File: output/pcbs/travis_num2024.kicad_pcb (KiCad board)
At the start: 2 copper layers, 85.2 x 132.8 mm, 91 parts

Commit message: numpad cap and firmware
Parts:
- C1: value 470uF 10V -> 6.3V 1000uF; footprint CP_Elec_6.3x7.7 -> Capacitor_THT:C_Radial_D6.3mm_H11.0mm_P2.50mm
- moved C1 1.25 mm to (37.0, 93.6), turned to 270 degrees
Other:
- board text added: "2024.06.20"
- board text removed: "2024.05.15"

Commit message: rotated
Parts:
- moved D15 20.8 mm to (106.3, 198.4), turned to 180 degrees
- moved D16 20.8 mm to (106.3, 158.3), turned to 180 degrees
- moved D1 20.8 mm to (41.6, 206.1), turned to 90 degrees
- moved D2 20.8 mm to (31.6, 186.1), turned to 90 degrees
- moved D3 20.8 mm to (31.6, 166.0), turned to 90 degrees
- moved D4 20.8 mm to (31.6, 146.0), turned to 90 degrees
- moved D5 20.8 mm to (31.6, 125.9), turned to 90 degrees
- moved D10 20.8 mm to (71.7, 206.1), turned to 90 degrees
- moved D11 20.8 mm to (71.7, 186.1), turned to 90 degrees
- moved D12 20.8 mm to (71.7, 166.0), turned to 90 degrees
- moved D13 20.8 mm to (71.7, 146.0), turned to 90 degrees
- moved D14 20.8 mm to (71.7, 125.9), turned to 90 degrees
- moved D17 20.8 mm to (91.7, 125.9), turned to 90 degrees
- moved D6 20.8 mm to (51.6, 186.1), turned to 90 degrees
- moved D7 20.8 mm to (51.6, 166.0), turned to 90 degrees
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
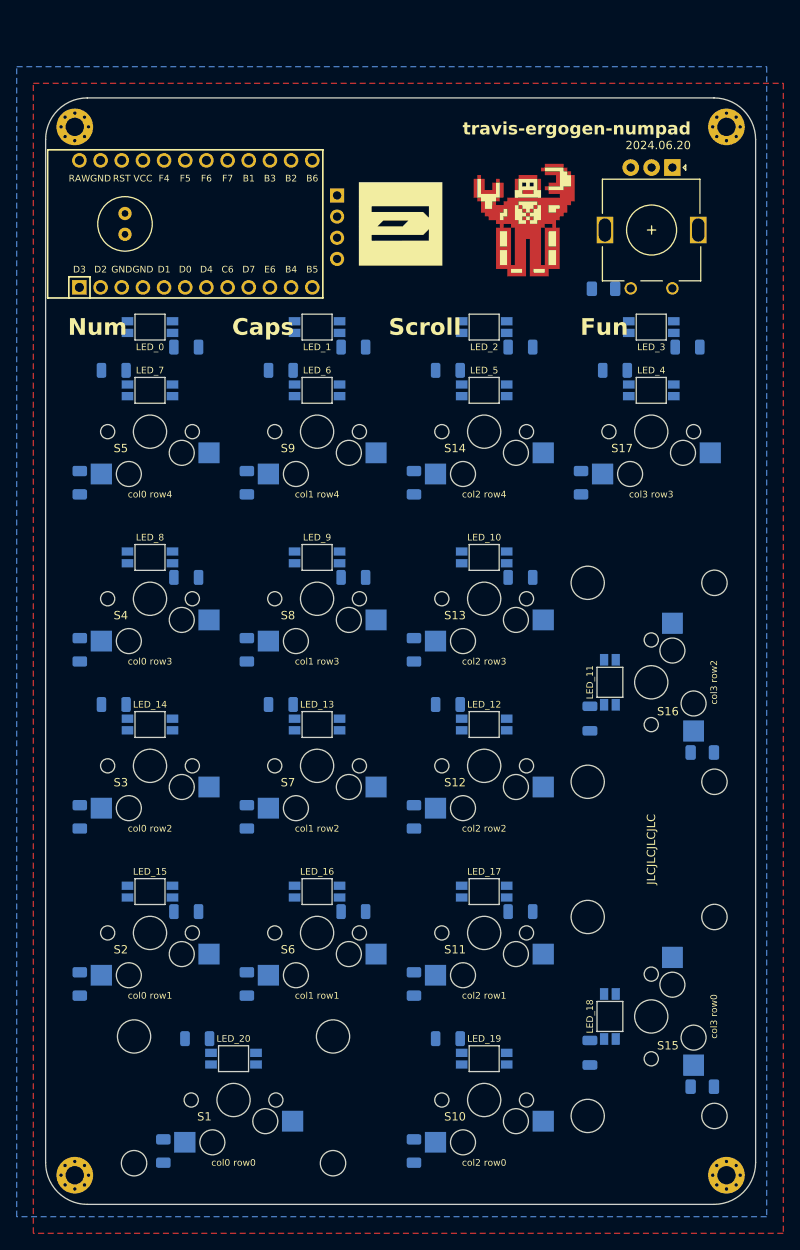
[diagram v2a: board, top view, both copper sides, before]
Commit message: added zones, fixed leds, caps
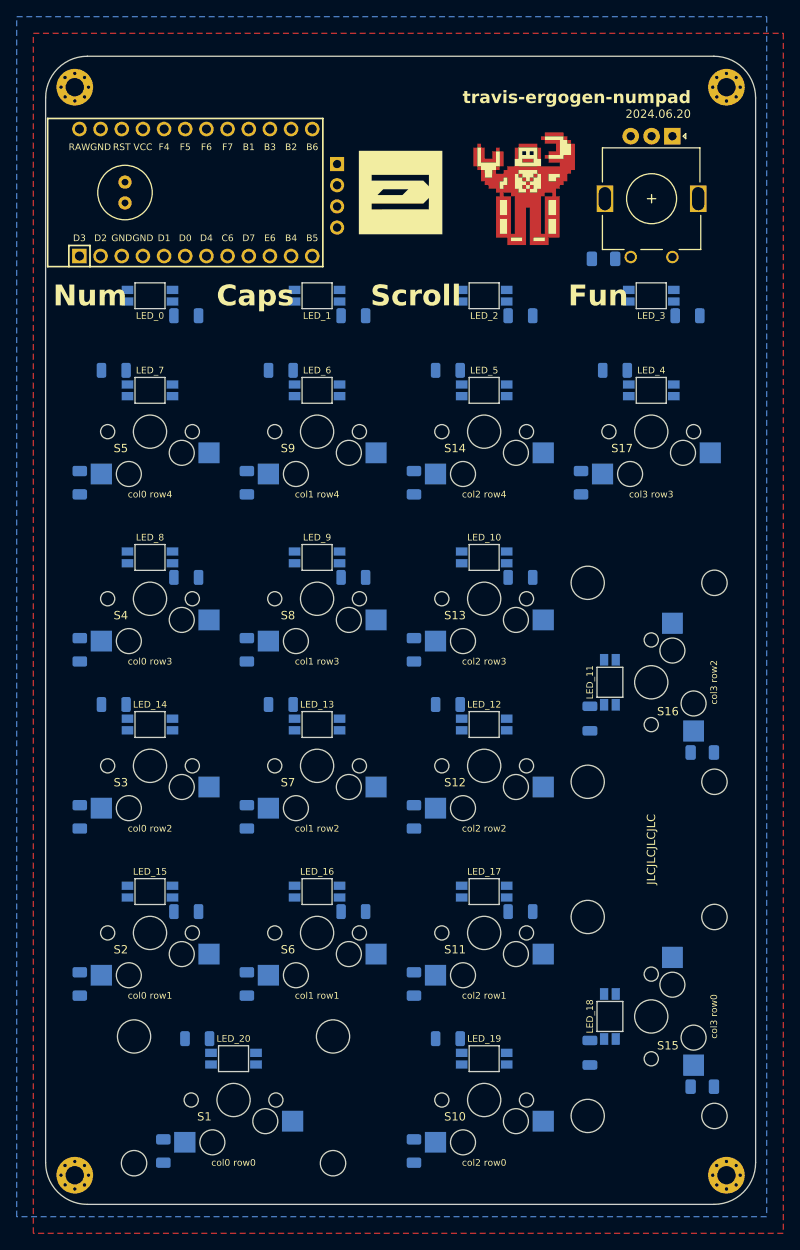
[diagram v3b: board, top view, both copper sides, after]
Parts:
- moved HOLE1 4.76 mm to (31.0, 78.5)
- moved HOLE2 4.76 mm to (109.2, 78.5)
- moved C1 3.76 mm to (37.0, 89.9)
- moved LOGO1 3.76 mm to (70.1, 91.1)
- moved LOGO2 3.76 mm to (85.1, 91.1)
- moved MCU1 3.76 mm to (45.5, 91.1)
- moved ROC1 3.76 mm to (70.1, 91.1)
- moved C2 3.76 mm to (44.4, 105.9)
- moved C3 3.76 mm to (64.4, 105.9)
- moved C4 3.76 mm to (84.4, 105.9)
- moved C5 3.76 mm to (104.5, 105.9)
- moved LED1 3.76 mm to (40.0, 103.5)
- moved LED2 3.76 mm to (60.0, 103.5)
- moved LED3 3.76 mm to (80.1, 103.5)
- moved LED4 3.76 mm to (100.2, 103.5)
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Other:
- board size 85.2 x 132.8 mm -> 85.2 x 137.8 mm

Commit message: routed v2
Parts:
- moved STAB2u1 0.60 mm to (50.0, 200.0), turned to 0 degrees
- moved STAB2u2 0.60 mm to (100.2, 190.0), turned to 90 degrees
- moved STAB2u3 0.60 mm to (100.2, 149.9), turned to 90 degrees
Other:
- board text added: "2024.06.23"
- board text removed: "2024.06.20"
